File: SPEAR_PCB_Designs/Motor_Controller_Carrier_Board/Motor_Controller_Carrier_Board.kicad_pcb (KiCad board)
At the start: 2 copper layers, 104 x 47 mm, 18 parts, among them J1 Conn_01x02_Pin, J2 Conn_01x02_Pin, J3 Conn_01x02_Pin, J4 JST_S4B-XH-A-1, U1 AP63203WU

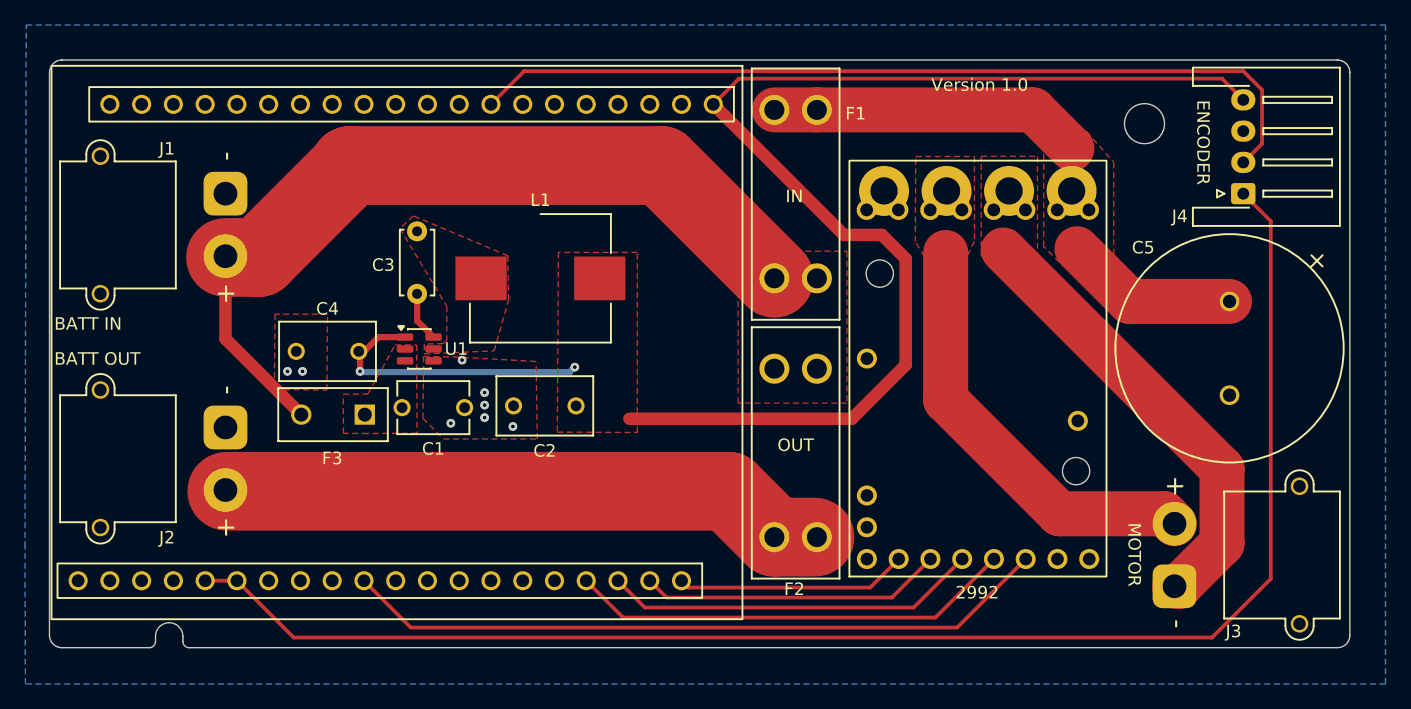
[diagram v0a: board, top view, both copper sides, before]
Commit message: Added board-to-board connectors to schematic and swapped out THT capacitors for SMT ones in carrier board
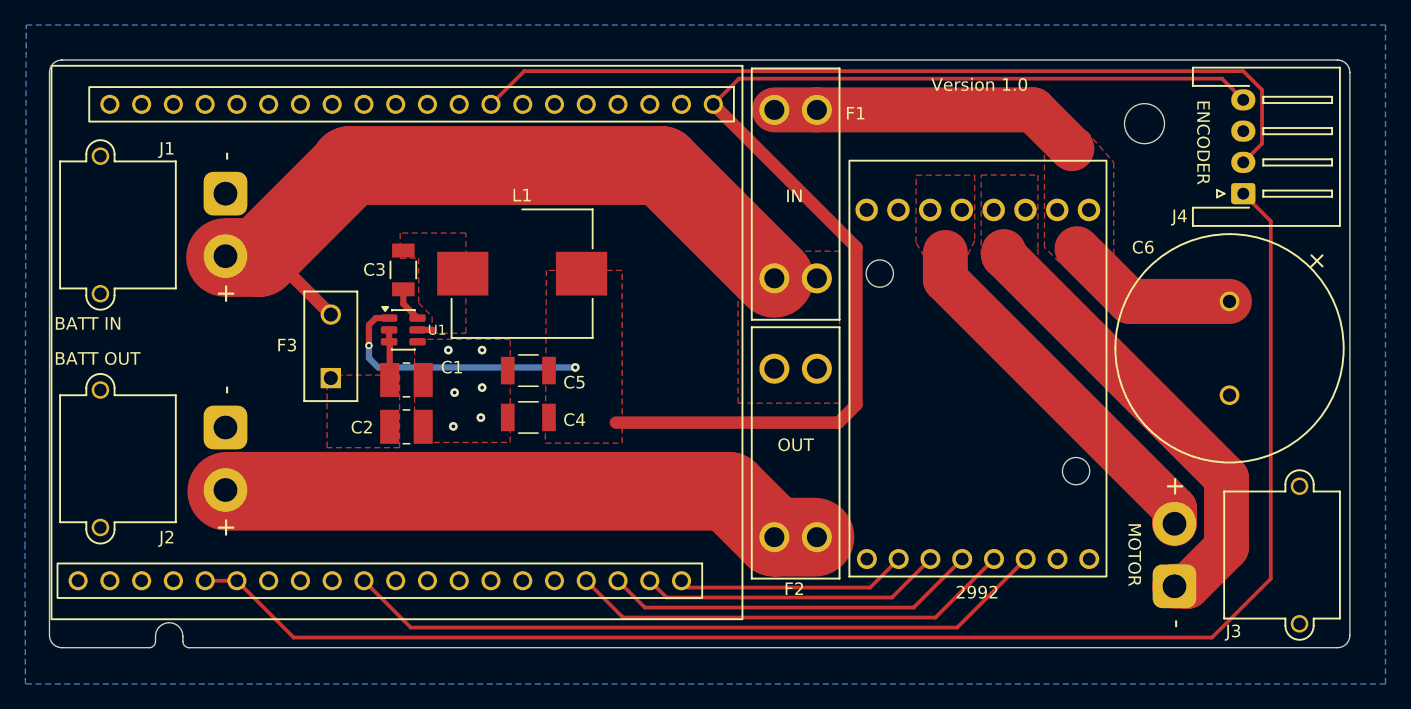
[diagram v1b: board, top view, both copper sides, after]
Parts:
- added C5: 22uF, Motor_Controller_Carrier_Board:CAP_C3225X7R1C226M250AC, F.Cu at (123.3, 93.8)
- C1: value 10u -> 10uF; footprint SPEAR_AP63203BuckConverter:CAP_FG20_TDK_C1 -> Motor_Controller_Carrier_Board:CAPC3225X270N
- C2: value 22u -> 10uF; footprint SPEAR_AP63203BuckConverter:CAP_FG22_TDK_C2_C4 -> Motor_Controller_Carrier_Board:CAPC3225X270N
- C3: value 100n -> 150nF; footprint Motor_Controller_Carrier_Board:C_Disc_D5.0mm_W2.5mm_P5.00mm -> Motor_Controller_Carrier_Board:CAP_CC1206_YAG
- C4: value 22u -> 22uF; footprint SPEAR_AP63203BuckConverter:CAP_FG22_TDK_C2_C4 -> Motor_Controller_Carrier_Board:CAP_C3225X7R1C226M250AC
- C6: renamed from C5; value C -> 1000uF
- F1: value 3557-10 -> 10A
- F2: value 3557-15 -> 15A
- F3: value Fuse -> 2A
- J4: value JST_S4B-XH-A-1 -> Conn_01x04_Pin
- L1: value 3.9u -> 3.9uH
- moved C4 14.6 mm to (123.3, 97.6)
- moved C2 13.7 mm to (113.5, 98.3), turned to 0 degrees
- moved F3 3.99 mm to (107.5, 94.4), turned to 90 degrees
- moved C3 3.28 mm to (113.3, 85.8)
- moved C1 2.24 mm to (113.5, 94.6)
- moved U1 1.99 mm to (113.3, 90.6)
- moved L1 1.51 mm to (122.8, 86.1)
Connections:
- net /CS renamed /Schematic/CS
- net /DIR renamed /Schematic/DIR
- net /ENC_A renamed /Schematic/ENC_A
- net /ENC_B renamed /Schematic/ENC_B
- net /FLT renamed /Schematic/FLT
- net /PWM renamed /Schematic/PWM
- net /SLP renamed /Schematic/SLP
- net /SW renamed /Schematic/SW
- net Net-(U1-BST) renamed /Schematic/BST
- C1 pad 1: /BUCK_PWR -> /Schematic/BUCK_PWR
- C2 pad 1: +3.3V -> /Schematic/BUCK_PWR
- C6 pad 1: /DRIVER_PWR -> /Schematic/DRIVER_PWR
- F1 pad 2_1: /DRIVER_PWR -> /Schematic/DRIVER_PWR
- F1 pad 2_2: /DRIVER_PWR -> /Schematic/DRIVER_PWR
- F3 pad 1: /BUCK_PWR -> /Schematic/BUCK_PWR
- MDB1 pad 10: unconnected-(MDB1-VREF-Pad10) -> GND
- MDB1 pad 11: GND -> Net-(J3-Pin_2)
- MDB1 pad 12: GND -> Net-(J3-Pin_2)
- MDB1 pad 13: GND -> Net-(J3-Pin_1)
- MDB1 pad 14: GND -> Net-(J3-Pin_1)
- MDB1 pad 15: GND -> /Schematic/DRIVER_PWR
- MDB1 pad 16: Net-(J3-Pin_2) -> /Schematic/DRIVER_PWR
- U1 pad 2: /BUCK_PWR -> /Schematic/BUCK_PWR
- U1 pad 3: /BUCK_PWR -> /Schematic/BUCK_PWR
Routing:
- net /Schematic/DRIVER_PWR: track 0.00 -> 39.0 mm
- net /DRIVER_PWR: track 39.0 -> 0.00 mm
- net Net-(J1-Pin_2): track 65.9 -> 57.3 mm
- net +3.3V: track 120.1 -> 113.8 mm
- net Net-(J3-Pin_2): track 34.2 -> 29.3 mm
- net /Schematic/BUCK_PWR: track 0.00 -> 4.02 mm
- net /Schematic/SW: track 0.00 -> 1.25 mm
- net /Schematic/BST: track 4.00 -> 2.77 mm
- net Net-(J3-Pin_1): track 35.9 -> 36.5 mm
- net GND: vias 8 -> 6
- added copper zone on F.Cu, net /Schematic/BUCK_PWR
- added copper zone on F.Cu, net /Schematic/DRIVER_PWR
- removed copper zone on F.Cu, net /BUCK_PWR
- removed copper zone on F.Cu, net /DRIVER_PWR

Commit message: Generated gerbers for carrier board with new buck converter layout
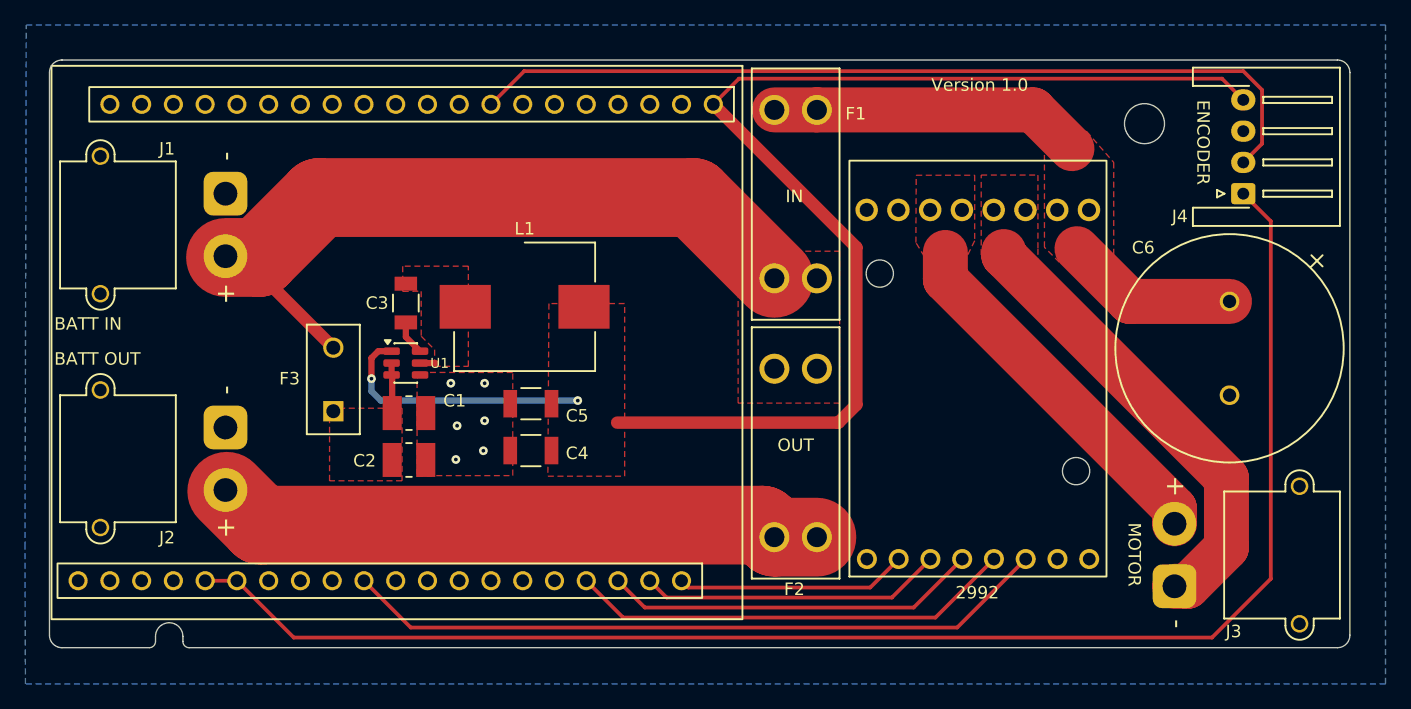
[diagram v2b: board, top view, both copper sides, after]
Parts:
- moved G*** 6.46 mm to (116.6, 82.7)
- moved C1 2.66 mm to (113.8, 97.2)
- moved C2 2.66 mm to (113.8, 101.0)
- moved C4 2.66 mm to (123.5, 100.2)
- moved C5 2.66 mm to (123.5, 96.5)
- moved L1 2.66 mm to (123.0, 88.7)
- moved U1 2.66 mm to (113.5, 93.2)
- moved C3 2.66 mm to (113.5, 88.4)
- moved F3 2.66 mm to (107.7, 97.1)
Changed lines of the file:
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@@
 	(footprint "Motor_Controller_Carrier_Board:CAPC3225X270N"
 		(layer "F.Cu")
-		(at 113.55 98.33675)
+		(at 113.75 100.98675)
 		(property "Reference" "C2"
 			(at -3.55 0.06325 0)
@@
 		(attr smd)
 		(fp_line
-			(start -0.26 -1.35)
-			(end 0.26 -1.35)
+			(start -0.23 -1.35)
+			(end 0.23 -1.35)
 			(stroke
-				(width 0.127)
+				(width 0.15)
 				(type solid)
 			)
@@
 		)
 		(fp_line
-			(start -0.26 1.35)
-			(end 0.26 1.35)
+			(start -0.23 1.35)
+			(end 0.23 1.35)
 			(stroke
-				(width 0.127)
+				(width 0.15)
 				(type solid)
 			)
@@
 	(footprint "Motor_Controller_Carrier_Board:TSOT-23-6"
 		(layer "F.Cu")
-		(at 113.3 90.58675)
+		(at 113.5 93.23675)
 		(descr "TSOT, 6 Pin (https://www.jedec.org/sites/default/files/docs/MO-193D.pdf variant AA), generated with kicad-footprint-generator ipc_gullwing_generator.py")
 		(tags "TSOT TO_SOT_SMD")
@@
 	(footprint "Motor_Controller_Carrier_Board:FUS_LITTELFUSE_392_LTF"
 		(layer "F.Cu")
-		(at 107.5 94.43675 90)
+		(at 107.7 97.08675 90)
 		(tags "39212000000 ")
 		(property "Reference" "F3"
@@
 	(footprint "SPEAR_AP63203BuckConverter:L_Wurth_WE-LHMI-1040_L1"
 		(layer "F.Cu")
-		(at 122.8 86.08675)
+		(at 123 88.73675)
 		(descr "Shielded Power Inductor, body 11x10x3.8mm, https://www.we-online.com/en/components/products/WE-LHMI#/articles/WE-LHMI-1040")
 		(tags "SMT")
@@
 			(polygon
 				(pts
-					(xy 120.1 91.33675) (xy 125.5 91.33675) (xy 125.5 80.83675) (xy 120.1 80.83675)
+					(xy 120.3 93.98675) (xy 125.7 93.98675) (xy 125.7 83.48675) (xy 120.3 83.48675)
 				)
 			)
@@
 	(footprint "Motor_Controller_Carrier_Board:CAP_C3225X7R1C226M250AC"
 		(layer "F.Cu")
-		(at 123.3 97.58675 180)
+		(at 123.5 100.23675 180)
 		(property "Reference" "C4"
 			(at -3.7 -0.21325 0)
@@
 			(end 0.78 1.25)
 			(stroke
-				(width 0.127)
+				(width 0.15)
 				(type solid)
 			)
@@
 			(end 0.78 -1.25)
 			(stroke
-				(width 0.127)
+				(width 0.15)
 				(type solid)
 			)
@@
 	(footprint "Motor_Controller_Carrier_Board:CAPC3225X270N"
 		(layer "F.Cu")
-		(at 113.55 94.58675)
+		(at 113.75 97.23675)
 		(property "Reference" "C1"
 			(at 3.65 -0.98675 0)
@@
 		(attr smd)
 		(fp_line
-			(start -0.26 -1.35)
-			(end 0.26 -1.35)
+			(start -0.23 -1.35)
+			(end 0.23 -1.35)
 			(stroke
-				(width 0.127)
+				(width 0.15)
 				(type solid)
 			)
@@
 		)
 		(fp_line
-			(start -0.26 1.35)
-			(end 0.26 1.35)
+			(start -0.23 1.35)
+			(end 0.23 1.35)
 			(stroke
-				(width 0.127)
+				(width 0.15)
 				(type solid)
 			)
@@
 	(footprint "Motor_Controller_Carrier_Board:CAP_CC1206_YAG"
 		(layer "F.Cu")
-		(at 113.3 85.78735 -90)
+		(at 113.5 88.43735 -90)
 		(tags "CC1206KRX7R8BB154 ")
 		(property "Reference" "C3"
@@
 			(polygon
 				(pts
-					(xy 114.1509 84.84755) (xy 114.1509 86.72715) (xy 112.4491 86.72715) (xy 112.4491 84.84755)
+					(xy 114.3509 87.49755) (xy 114.3509 89.37715) (xy 112.6491 89.37715) (xy 112.6491 87.49755)
 				)
 			)
@@
 	(footprint "Motor_Controller_Carrier_Board:CAP_C3225X7R1C226M250AC"
 		(layer "F.Cu")
-		(at 123.3 93.83675 180)
+		(at 123.5 96.48675 180)
 		(property "Reference" "C5"
 			(at -3.7 -0.96325 0)
@@
 			(end 0.78 1.25)
 			(stroke
-				(width 0.127)
+				(width 0.15)
 				(type solid)
 			)
@@
 			(end 0.78 -1.25)
 			(stroke
-				(width 0.127)
+				(width 0.15)
 				(type solid)
 			)
@@
 	(footprint "SPEAR_Logos:spear_logo_10.0x10"
 		(layer "B.Cu")
-		(at 122.6 80.3 180)
+		(at 116.6 82.7 180)
 		(property "Reference" "G***"
 			(at 0 0 0)
@@
 	)
 	(gr_text "Oliver Schneider\nRonak Grover\nHenry Diep"
-		(at 135.8 80.3 0)
+		(at 129.8 82.7 0)
 		(layer "B.SilkS")
 		(effects
@@
 	)
 	(via
-		(at 117.3 98.3)
+		(at 117.5 100.95)
 		(size 0.7)
 		(drill 0.3)
@@
 	)
 	(via
-		(at 119.6 92.2)
+		(at 119.8 94.85)
 		(size 0.7)
 		(drill 0.3)
@@
 	)
 	(via
-		(at 119.6 95.2)
+		(at 119.8 97.85)
 		(size 0.7)
 		(drill 0.3)
@@
 	)
 	(via
-		(at 116.9 92.2)
+		(at 117.1 94.85)
 		(size 0.7)
 		(drill 0.3)
@@
 	)
 	(via
-		(at 119.5 97.6)
+		(at 119.7 100.25)
 		(size 0.7)
 		(drill 0.3)
@@
 	)
 	(via
-		(at 117.4 95.6)
+		(at 117.6 98.25)
 		(size 0.7)
 		(drill 0.3)
@@
 	(segment
 		(start 142.975 107.159442)
-		(end 139.306 103.490442)
+		(end 146.375 107.159442)
 		(width 6.3)
 		(layer "F.Cu")
@@
 	)
 	(segment
-		(start 139.306 103.490442)
-		(end 99.176 103.490442)
+		(start 142.975 107.159442)
+		(end 142.015558 106.2)
 		(width 6.3)
 		(layer "F.Cu")
@@
 	)
 	(segment
-		(start 142.975 107.159442)
-		(end 146.224 107.159442)
+		(start 142.015558 106.2)
+		(end 101.885558 106.2)
 		(width 6.3)
 		(layer "F.Cu")
@@
 	)
 	(segment
-		(start 110.55 91.83675)
-		(end 110.55 90.18675)
+		(start 101.885558 106.2)
+		(end 99.176 103.490442)
+		(width 6.3)
+		(layer "F.Cu")
+		(net 3)
+	)
+	(segment
+		(start 110.75 94.48675)
+		(end 110.75 92.83675)
 		(width 0.5)
 		(layer "F.Cu")
@@
 	)
 	(segment
-		(start 148.1 98)
-		(end 130.3 98)
-		(width 1)
-		(layer "F.Cu")
-		(net 4)
-	)
-	(segment
 		(start 180.475 72.189442)
 		(end 178.775 70.489442)
@@
 	)
 	(segment
+		(start 148.1 98)
+		(end 130.4 98)
+		(width 1)
+		(layer "F.Cu")
+		(net 4)
+	)
+	(segment
 		(start 149.53 96.57)
 		(end 148.1 98)
@@
 	)
 	(segment
-		(start 110.55 90.18675)
-		(end 111.1 89.63675)
+		(start 110.75 92.83675)
+		(end 111.3 92.28675)
 		(width 0.5)
 		(layer "F.Cu")
@@
 	)
 	(segment
-		(start 111.1 89.63675)
-		(end 112.1625 89.63675)
+		(start 111.3 92.28675)
+		(end 112.3625 92.28675)
 		(width 0.5)
 		(layer "F.Cu")
@@
 	)
 	(via
-		(at 110.55 91.83675)
-		(size 0.6)
+		(at 110.75 94.48675)
+		(size 0.7)
 		(drill 0.3)
 		(layers "F.Cu" "B.Cu")
@@
 	)
 	(via
-		(at 127.05 93.58675)
+		(at 127.25 96.23675)
 		(size 0.7)
 		(drill 0.3)
@@
 	)
 	(segment
-		(start 111.3 93.58675)
-		(end 110.55 92.83675)
+		(start 111.5 96.23675)
+		(end 110.75 95.48675)
 		(width 0.5)
 		(layer "B.Cu")
@@
 	)
 	(segment
-		(start 127.05 93.58675)
-		(end 111.3 93.58675)
+		(start 127.25 96.23675)
+		(end 111.5 96.23675)
 		(width 0.5)
 		(layer "B.Cu")
@@
 	)
 	(segment
-		(start 110.55 92.83675)
-		(end 110.55 91.83675)
+		(start 110.75 95.48675)
+		(end 110.75 94.48675)
 		(width 0.5)
 		(layer "B.Cu")
@@
 	)
 	(segment
-		(start 109.013974 77.438442)
-		(end 109.013974 77.538442)
-		(width 6.3)
-		(layer "F.Cu")
-		(net 37)
-	)
-	(segment
-		(start 101.761974 84.790442)
-		(end 99.075 84.790442)
+		(start 106.552416 80)
+		(end 101.761974 84.790442)
 		(width 6.3)
 		(layer "F.Cu")
@@
 	)
 	(segment
-		(start 142.975 86.459442)
-		(end 133.954 77.438442)
+		(start 136.515558 80)
+		(end 106.552416 80)
 		(width 6.3)
 		(layer "F.Cu")
@@
 	)
 	(segment
-		(start 102.832692 84.689442)
-		(end 107.5 89.35675)
+		(start 107.7 92.00675)
+		(end 101.761974 86.068724)
 		(width 1)
 		(layer "F.Cu")
@@
 	)
 	(segment
-		(start 109.013974 77.538442)
-		(end 101.761974 84.790442)
+		(start 142.975 86.459442)
+		(end 136.515558 80)
 		(width 6.3)
 		(layer "F.Cu")
@@
 	)
 	(segment
-		(start 133.954 77.438442)
-		(end 109.013974 77.438442)
+		(start 101.761974 84.790442)
+		(end 99.075 84.790442)
 		(width 6.3)
 		(layer "F.Cu")
@@
 	)
 	(segment
-		(start 112.209 91.58325)
-		(end 112.1625 91.53675)
+		(start 112.409 94.23325)
+		(end 112.3625 94.18675)
 		(width 0.5)
 		(layer "F.Cu")
@@
 	)
 	(segment
-		(start 112.209 94.58675)
-		(end 112.209 91.58325)
+		(start 112.409 97.23675)
+		(end 112.409 94.23325)
 		(width 0.5)
 		(layer "F.Cu")
@@
 	)
 	(segment
-		(start 112.1625 91.53675)
-		(end 112.1625 90.58675)
+		(start 112.3625 94.18675)
+		(end 112.3625 93.23675)
 		(width 0.5)
 		(layer "F.Cu")
@@
 	)
 	(segment
-		(start 114.4375 90.58675)
-		(end 115.68675 90.58675)
+		(start 114.6375 93.23675)
+		(end 115.88675 93.23675)
 		(width 0.5)
 		(layer "F.Cu")
@@
 	)
 	(segment
-		(start 114.4375 89.63675)
-		(end 113.3 88.49925)
+		(start 114.6375 92.28675)
+		(end 113.5 91.14925)
 		(width 0.5)
 		(layer "F.Cu")
@@
 	)
 	(segment
-		(start 113.3 88.49925)
-		(end 113.3 87.33675)
+		(start 113.5 91.14925)
+		(end 113.5 89.98675)
 		(width 0.5)
 		(layer "F.Cu")
@@
 		(polygon
 			(pts
-				(xy 118.3 90.85) (xy 118.3 82.83675) (xy 113.05 82.83675) (xy 113.05 84.851785) (xy 114.524986 84.839291)
-				(xy 114.529893 88.441038) (xy 115.6 89.514719) (xy 115.6 90.85)
+				(xy 118.5 93.5) (xy 118.5 85.48675) (xy 113.25 85.48675) (xy 113.25 87.501785) (xy 114.724986 87.489291)
+				(xy 114.729893 91.091038) (xy 115.8 92.164719) (xy 115.8 93.5)
 			)
 		)
@@
 		(polygon
 			(pts
-				(xy 107.2 94.2) (xy 113 94.2) (xy 113 100) (xy 107.2 100)
+				(xy 107.4 96.85) (xy 113.2 96.85) (xy 113.2 102.65) (xy 107.4 102.65)
 			)
 		)
@@
 		(polygon
 			(pts
-				(xy 114.2 91.33675) (xy 114.2 99.58675) (xy 121.85 99.58675) (xy 121.85 91.33675)
+				(xy 114.4 93.98675) (xy 114.4 102.23675) (xy 122.05 102.23675) (xy 122.05 93.98675)
 			)
 		)
@@
 		(polygon
 			(pts
-				(xy 124.658105 99.63675) (xy 130.8 99.63675) (xy 130.8 85.826192) (xy 124.742446 85.826192)
+				(xy 124.858105 102.28675) (xy 131 102.28675) (xy 131 88.476192) (xy 124.942446 88.476192)
 			)
 		)
